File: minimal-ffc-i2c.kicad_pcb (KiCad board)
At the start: 2 copper layers, 11.5 x 13.8 mm, 4 parts, among them J1 Conn_01x04_Female, J2 Conn_01x12_Female

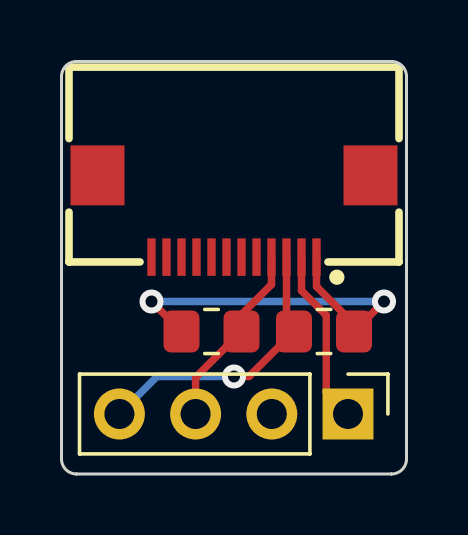
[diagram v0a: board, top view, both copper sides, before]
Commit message: vcc fix
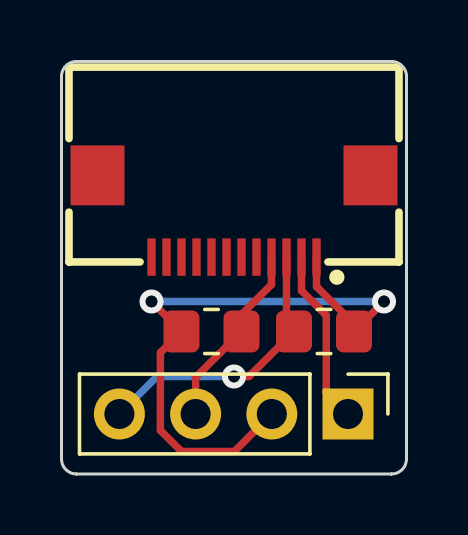
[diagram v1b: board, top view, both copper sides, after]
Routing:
- net vcc: track 13.6 -> 21.7 mm
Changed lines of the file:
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@@
   (setup
     (pad_to_mask_clearance 0)
+    (grid_origin 109.15 95.05)
     (pcbplotparams
       (layerselection 0x00010fc_ffffffff)
@@
       (outputformat 1)
       (mirror false)
-      (drillshape 1)
+      (drillshape 0)
       (scaleselection 1)
-      (outputdirectory "")
+      (outputdirectory "/Users/tombarnes/Documents/GitHub/hardware-gits/minimal-ffc-i2c/tidygit/Untitled/pcba/gerber/")
     )
   )
@@
     (fp_line (start 1 -0.625) (end 1 0.625) (layer "F.Fab") (width 0.1))
     (fp_line (start 1 0.625) (end -1 0.625) (layer "F.Fab") (width 0.1))
-    (pad "1" smd roundrect (at -1 0 180) (size 1.2 1.4) (layers "F.Cu" "F.Paste" "F.Mask") (roundrect_rratio 0.208333)
+    (pad "1" smd roundrect (at -1 0 180) (size 1.2 1.4) (layers "F.Cu" "F.Paste" "F.Mask") (roundrect_rratio 0.2083333333)
       (net 3 "sck") (pintype "passive"))
-    (pad "2" smd roundrect (at 1 0 180) (size 1.2 1.4) (layers "F.Cu" "F.Paste" "F.Mask") (roundrect_rratio 0.208333)
+    (pad "2" smd roundrect (at 1 0 180) (size 1.2 1.4) (layers "F.Cu" "F.Paste" "F.Mask") (roundrect_rratio 0.2083333333)
       (net 2 "vcc") (pintype "passive"))
     (model "${KICAD6_3DMODEL_DIR}/Resistor_SMD.3dshapes/R_0805_2012Metric.wrl"
@@
     (fp_line (start 1 -0.625) (end 1 0.625) (layer "F.Fab") (width 0.1))
     (fp_line (start -1 -0.625) (end 1 -0.625) (layer "F.Fab") (width 0.1))
-    (pad "1" smd roundrect (at -1 0) (size 1.2 1.4) (layers "F.Cu" "F.Paste" "F.Mask") (roundrect_rratio 0.208333)
+    (pad "1" smd roundrect (at -1 0) (size 1.2 1.4) (layers "F.Cu" "F.Paste" "F.Mask") (roundrect_rratio 0.2083333333)
       (net 4 "sda") (pintype "passive"))
-    (pad "2" smd roundrect (at 1 0) (size 1.2 1.4) (layers "F.Cu" "F.Paste" "F.Mask") (roundrect_rratio 0.208333)
+    (pad "2" smd roundrect (at 1 0) (size 1.2 1.4) (layers "F.Cu" "F.Paste" "F.Mask") (roundrect_rratio 0.2083333333)
       (net 2 "vcc") (pintype "passive"))
     (model "${KICAD6_3DMODEL_DIR}/Resistor_SMD.3dshapes/R_0805_2012Metric.wrl"
@@
   (segment (start 114 94.637507) (end 114.82548 95.462987) (width 0.25) (layer "F.Cu") (net 1))
   (segment (start 114.5 93.52) (end 114.5 94.501789) (width 0.25) (layer "F.Cu") (net 2))
+  (segment (start 110 96) (end 109.295489 96.704511) (width 0.25) (layer "F.Cu") (net 2))
+  (segment (start 111.76 100) (end 113.01 98.75) (width 0.25) (layer "F.Cu") (net 2))
   (segment (start 110 96) (end 109 95) (width 0.25) (layer "F.Cu") (net 2))
   (segment (start 116.75 95) (end 115.75 96) (width 0.25) (layer "F.Cu") (net 2))
+  (segment (start 109.295489 99.295489) (end 110 100) (width 0.25) (layer "F.Cu") (net 2))
   (segment (start 114.5 94.501789) (end 115.75 95.751789) (width 0.25) (layer "F.Cu") (net 2))
   (segment (start 115.75 95.751789) (end 115.75 96) (width 0.25) (layer "F.Cu") (net 2))
+  (segment (start 109.295489 96.704511) (end 109.295489 99.295489) (width 0.25) (layer "F.Cu") (net 2))
+  (segment (start 110 100) (end 111.76 100) (width 0.25) (layer "F.Cu") (net 2))
   (via (at 116.75 95) (size 0.8) (drill 0.4) (layers "F.Cu" "B.Cu") (net 2))
   (via (at 109 95) (size 0.8) (drill 0.4) (layers "F.Cu" "B.Cu") (net 2))
